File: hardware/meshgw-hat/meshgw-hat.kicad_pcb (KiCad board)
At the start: 2 copper layers, 65 x 56.5 mm, 9 parts, among them J1 RPi_GPIO40, U1 E22-900M30S

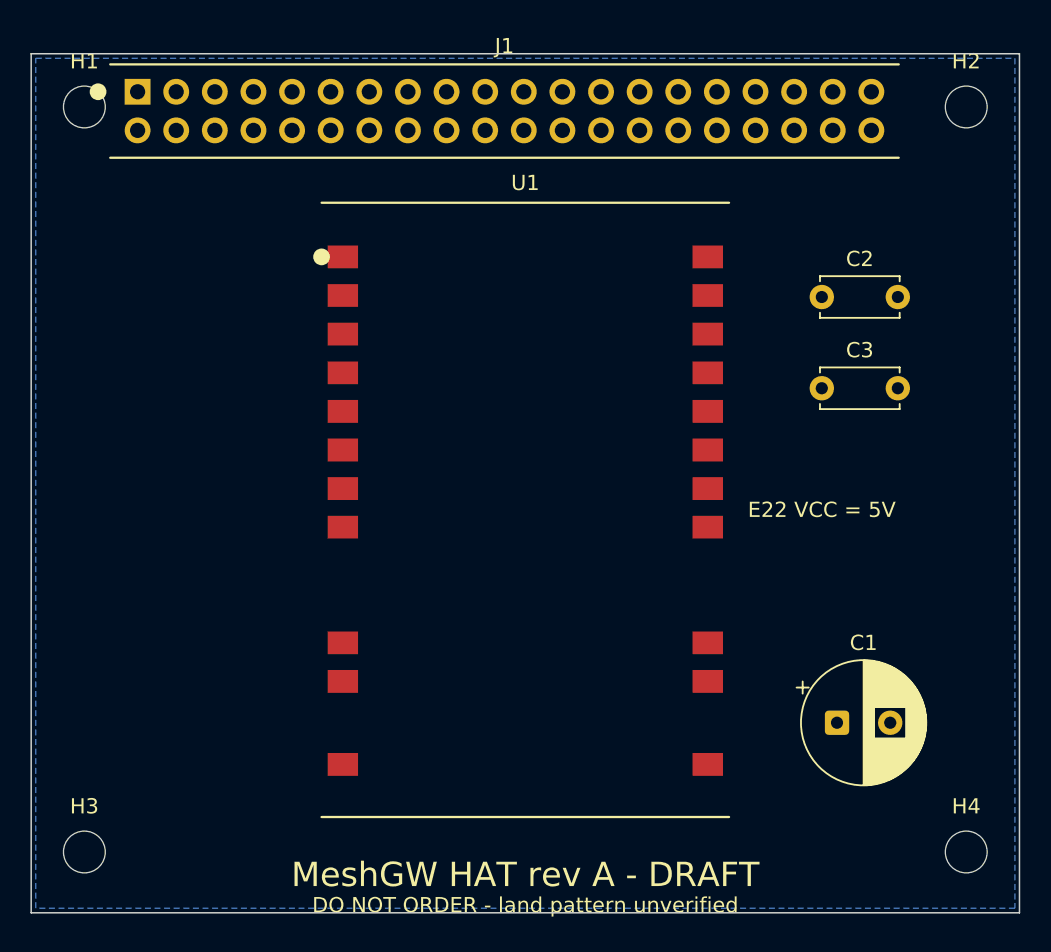
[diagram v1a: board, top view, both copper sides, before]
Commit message: meshgw HAT: verify mechanical geometry vs Pi 3B+, unify netlist, fix schematic short
The HAT geometry was unverified against the official Raspberry Pi HAT spec,
as route.sh itself warned. Verified against three independent sources (the
HAT mechanical PDF, the Pi 3B+ drawing, and KiCad's own HAT template plus its
Pi Zero socketed footprint). It was wrong six ways while passing DRC with
0 violations and 0 unconnected:

  - header rows swapped: every SPI signal onto its neighbour's pin
  - header origin (7.0, 2.5) instead of (8.37, 4.77): would not seat at all
  - 56.5 mm tall: that is the SMT-header figure, through-hole needs 56.0
  - square corners against a spec mandating R3
  - pour flooded to 0.5 mm of mounting holes needing a 6.2 mm isolated land
  - no clearance for the Pi 3B+ PoE header J14

J14 gets an edge-open notch rather than an enclosed cutout: it leaves ~1 mm
to the board edge, and it can carry ~48-57 V on a PoE switch.

New check_geometry.py asserts 27 of these facts against the ROUTED board and
route.sh runs it, because a clean DRC is not a negative control for geometry.

New netlist.py is the single pinout source. gen.py and gen_pcb.py each held a
copy 'mirroring' each other and had silently stopped; config/meshtasticd/
config.yaml had the old map too. GPIO map re-pinned off the MeshAdv-Pi-Hat
reference onto odd (inner-row) header pins -- forced, because four nets could
not be routed otherwise, and kept because GPIO5 idles chip-select deselected
where GPIO21 asserted it on every boot.

Separately, the SCHEMATIC had no GND net at all: C1/C2/C3 sat 5.08 mm apart
in a row, place() draws a 2.54 mm stub per pin, so adjacent stubs met and
shorted GND to +5V into a 27-node '+5V'. Invisible to every board-side check
because gen_pcb.py never reads the sheet. Caps stacked vertically, and
check_netlist.py now asserts the exported schematic netlist equals netlist.py.

Board: 119 segments, 0 vias, DRC 0/0, ERC 0, 27/27 mechanical checks.
Still DRAFT - DO NOT ORDER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
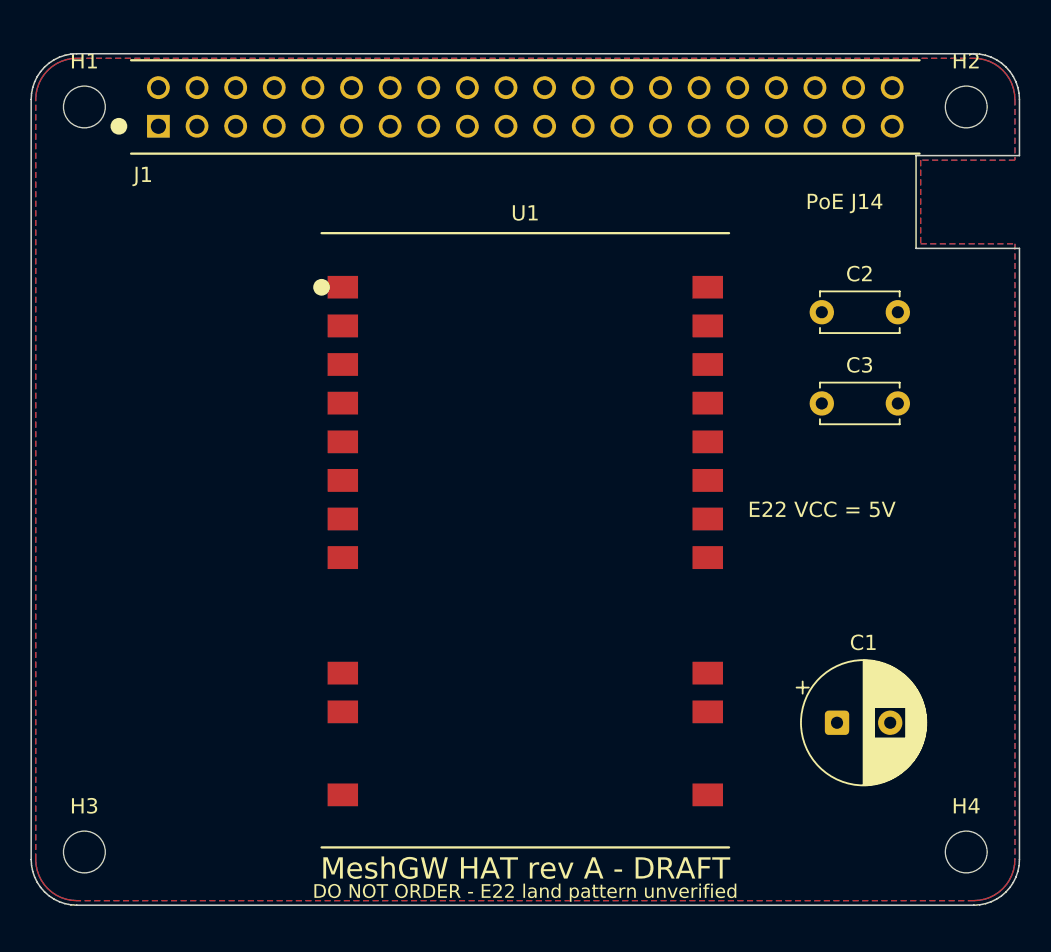
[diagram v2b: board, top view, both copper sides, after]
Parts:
- moved J1 2.65 mm to (108.4, 64.8)
- moved U1 2.00 mm to (132.5, 92.0)
- moved C2 1.00 mm to (152.0, 77.0)
- moved C3 1.00 mm to (152.0, 83.0)
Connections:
- J1 pad 11: (no net) -> DIO1
- J1 pad 12: NRST -> (no net)
- J1 pad 13: (no net) -> BUSY
- J1 pad 15: (no net) -> NRST
- J1 pad 29: (no net) -> NSS
- J1 pad 31: (no net) -> RXEN
- J1 pad 32: RXEN -> (no net)
- J1 pad 36: DIO1 -> (no net)
- J1 pad 38: BUSY -> (no net)
- J1 pad 40: NSS -> (no net)
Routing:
- added copper zone on F.Cu, net GND
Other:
- board size 65 x 56.5 mm -> 65 x 56 mm
- board text added: "DO NOT ORDER - E22 land pattern unverified"
- board text added: "PoE J14"
- board text removed: "DO NOT ORDER - land pattern unverified"

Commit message: meshgw HAT: clear rev A to order, build the fab package
Don's call 2026-08-12: batch the bare board into the shared JLCPCB checkout
with OSL, FD2, pool and Sentinel. Boards are ~$2 against $6-25 shipping, so
holding it back would pay that shipping charge again later with certainty.

U1's land pattern has still never met a physical module -- the E22 was ordered
the same day and is weeks out. fab_gate.py therefore keeps GEOMETRY_VERIFIED
False and carries a SEPARATE GEOMETRY_OVERRIDE string naming who decided, when
and why. Flipping the flag would have been one character and would have
destroyed the distinction between 'we checked' and 'we accepted the risk',
which is exactly what a reader six weeks from now needs.

The risk is real: the E22 solders to castellated pads, so a wrong land pattern
makes these boards scrap -- unlike Sentinel, whose open items were modules on
headers where a wrong guess costs a module, not a respin.

Silk changed from 'DO NOT ORDER - E22 land pattern unverified', which would be
false on a board ordered on purpose, to 'U1 LAND UNVERIFIED - CHECK FIT BEFORE
SOLDERING' -- a warning aimed at the moment it can still act. Checking a land
pattern is free before the iron and impossible after.

make_fab.sh follows Sentinel's, carrying its traps (PROTEL extensions not .gbr,
--excellon-units not --units, report-file DRC phrasing, board-file-derived
prefix) and adding a drill-size assert against JLCPCB's 0.30 mm minimum, which
nothing else in the chain checks. Smallest hole here is 0.80 mm.

Package: 12 members, every layer asserted by name, DRC and 27 mechanical
checks re-run on the fab copy rather than inherited.

Co-Authored-By: Claude Opus 5 <noreply@anthropic.com>
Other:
- board text added: "MeshGW HAT rev A"
- board text added: "U1 LAND UNVERIFIED - CHECK FIT BEFORE SOLDERING"
- board text removed: "DO NOT ORDER - E22 land pattern unverified"
- board text removed: "MeshGW HAT rev A - DRAFT"
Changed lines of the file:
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@@
 	)
 )
-  (gr_text "MeshGW HAT rev A - DRAFT" (at 132.5 113.6) (layer "F.SilkS") (effects (font (size 1.4 1.4) (thickness 0.2))))
-  (gr_text "DO NOT ORDER - E22 land pattern unverified" (at 132.5 115.1) (layer "F.SilkS") (effects (font (size 0.9 0.9) (thickness 0.15))))
+  (gr_text "MeshGW HAT rev A" (at 132.5 113.6) (layer "F.SilkS") (effects (font (size 1.4 1.4) (thickness 0.2))))
+  (gr_text "U1 LAND UNVERIFIED - CHECK FIT BEFORE SOLDERING" (at 132.5 115.1) (layer "F.SilkS") (effects (font (size 0.9 0.9) (thickness 0.15))))
   (gr_text "E22 VCC = 5V" (at 152.0 90.0) (layer "F.SilkS") (effects (font (size 1.0 1.0) (thickness 0.15))))
   (gr_text "PoE J14" (at 153.5 69.75) (layer "F.SilkS") (effects (font (size 1.0 1.0) (thickness 0.15))))
